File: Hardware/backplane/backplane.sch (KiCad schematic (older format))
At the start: 49 parts, among them J1 USB_B_Micro, SW1 SW_SPST, U1 74AC161, U2 MAX811SEUS-T, U3 MAX811SEUS-T, U4 PAL24, U5 74AC11, X1 24MHz

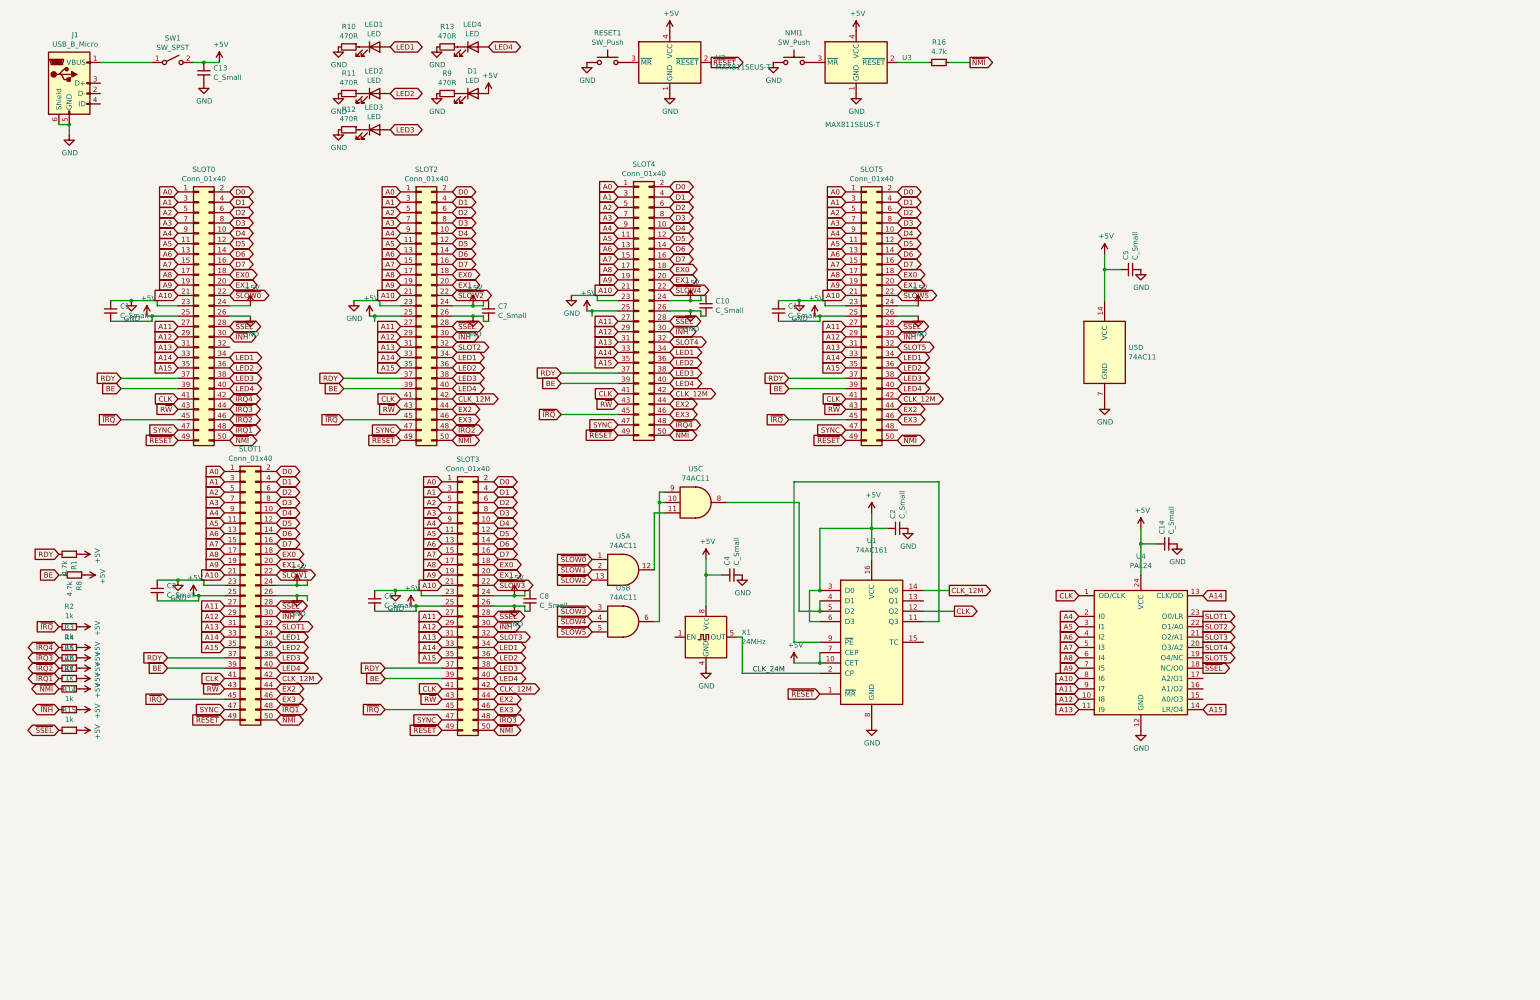
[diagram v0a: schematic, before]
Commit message: Many updates. SLOW signal is now shared amongst all slots, so their output has to be open drain.
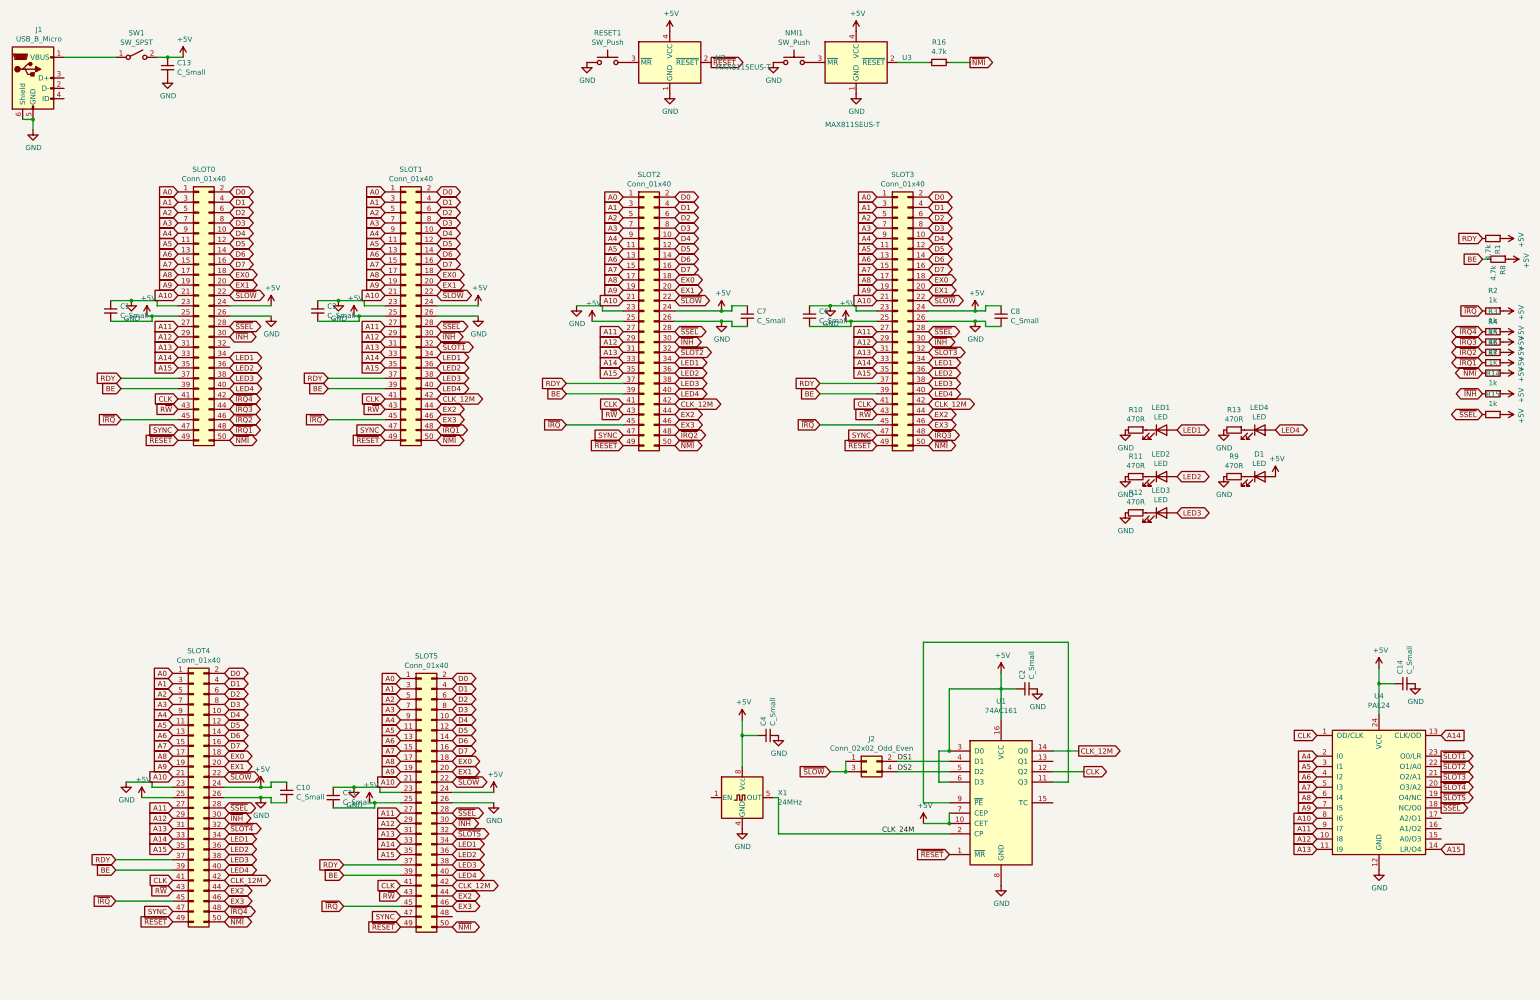
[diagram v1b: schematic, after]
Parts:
- removed C5: C_Small, Capacitor_SMD:C_1206_3216Metric_Pad1.42x1.75mm_HandSolder, symbol Device:C_Small
- removed U5: 74AC11, Package_SO:SOIC-14_3.9x8.7mm_P1.27mm, symbol 74xx:74LS11
- added J2: Conn_02x02_Odd_Even, Connector_PinHeader_2.54mm:PinHeader_2x02_P2.54mm_Vertical, symbol Connector_Generic:Conn_02x02_Odd_Even
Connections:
- net ~SLOW1~ is gone; now on net ~SLOW~: SLOT1.22 (Pin_22)
- net ~SLOW2~ is gone; now on net ~SLOW~: SLOT2.22 (Pin_22)
- net ~SLOW3~ is gone; now on net ~SLOW~: SLOT3.22 (Pin_22)
- net ~SLOW4~ is gone; now on net ~SLOW~: SLOT4.22 (Pin_22)
- net ~SLOW5~ is gone; now on net ~SLOW~: SLOT5.22 (Pin_22)
- net DS1: now reaches U1.4 (D1)
- net DS1: now also J2.2 (Pin_2); no longer U1.5 (D2)
- net SLOT1 renamed ~SLOT1~
- net SLOT2 renamed ~SLOT2~
- net SLOT3 renamed ~SLOT3~
- net SLOT4 renamed ~SLOT4~
- net SLOT5 renamed ~SLOT5~
- net ~SLOW0~ renamed ~SLOW~
- net ~SLOW~: now also J2.1 (Pin_1), J2.3 (Pin_3)
- new net DS2: J2.4 (Pin_4), U1.5 (D2)
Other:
- moved on the sheet: C10, C11, C13, C14, C2, C3, C4, C6, C7, C8, D1, J1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

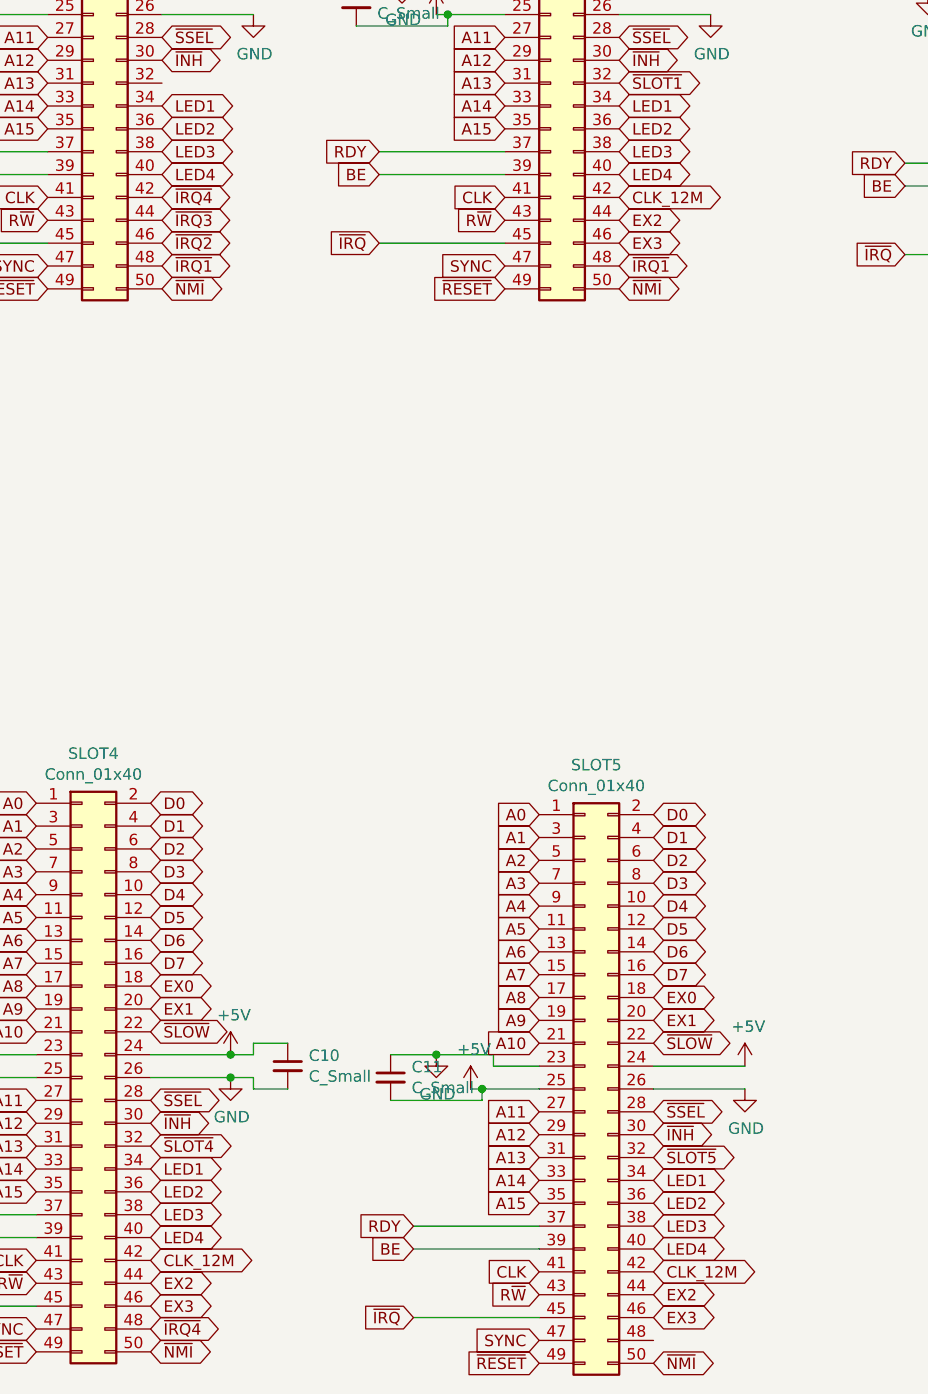
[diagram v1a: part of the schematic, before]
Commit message: Add IRQ signal for Slot 5
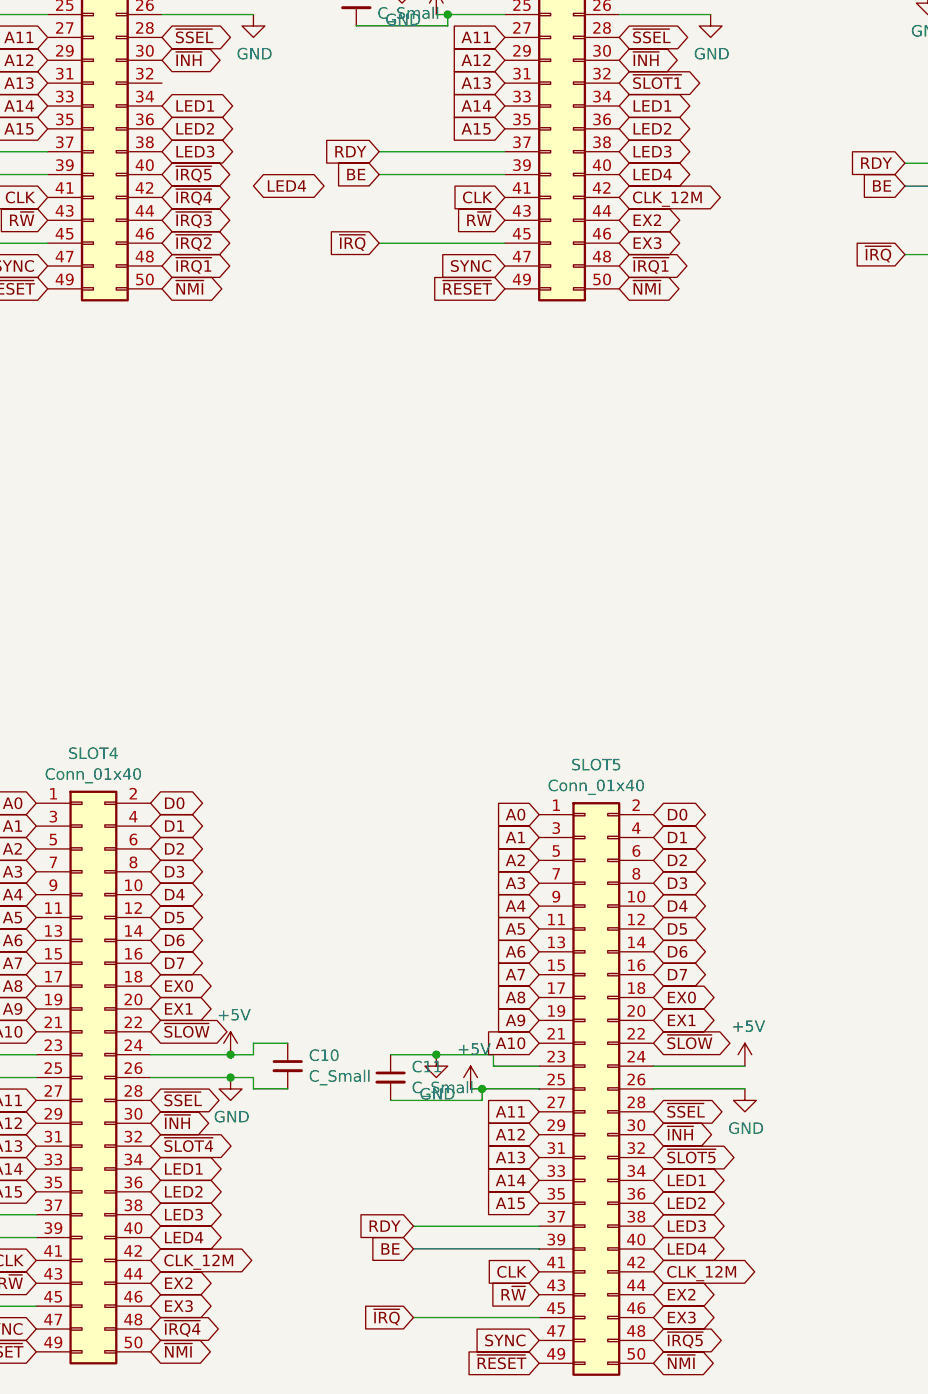
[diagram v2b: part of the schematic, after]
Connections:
- net LED4: no longer SLOT0.40 (Pin_40)
- net ~IRQ5~: now reaches SLOT5.48 (Pin_48)
- net ~IRQ5~: now also SLOT0.40 (Pin_40)
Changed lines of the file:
@@
 Text GLabel 2800 4150 2    50   BiDi ~ 0
 LED3
-Text GLabel 2800 4250 2    50   BiDi ~ 0
+Text GLabel 3200 4300 2    50   BiDi ~ 0
 LED4
 Text GLabel 2800 3150 2    50   BiDi ~ 0
@@
 Text Label 9250 7850 0    50   ~ 0
 DS1
+Text GLabel 2800 4250 2    50   BiDi ~ 0
+~IRQ5~
+Text GLabel 4950 9350 2    50   BiDi ~ 0
+~IRQ5~
 $EndSCHEMATC

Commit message: Backplane provides diode and pullups for SLOW signal
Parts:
- added D2, D3, D4, D5, D6, D7: DIODE, Diode_SMD:D_0805_2012Metric_Pad1.15x1.40mm_HandSolder, symbol pspice:DIODE
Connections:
- net ~IRQ~: no longer R2.2
- net ~SLOW~: now also R2.2, D2.1 (K), D3.1 (K), D4.1 (K), D5.1 (K), D6.1 (K), D7.1 (K); no longer SLOT0.22 (Pin_22), SLOT1.22 (Pin_22), SLOT2.22 (Pin_22), SLOT3.22 (Pin_22), SLOT4.22 (Pin_22), SLOT5.22 (Pin_22)
- new net: D3.2 (A), SLOT0.22 (Pin_22)
- new net: D6.2 (A), SLOT2.22 (Pin_22)
- new net: D2.2 (A), SLOT4.22 (Pin_22)
- new net: D5.2 (A), SLOT5.22 (Pin_22)
- new net: D4.2 (A), SLOT1.22 (Pin_22)
- new net: D7.2 (A), SLOT3.22 (Pin_22)
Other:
- note added: "Replace IRQ pull up with SLOW pullup"
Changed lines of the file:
@@
 ~IRQ1~
 Text GLabel 14900 3500 0    50   Input ~ 0
-~IRQ~
+~SLOW~
 Text GLabel 14900 2800 0    50   Input ~ 0
 RDY
@@
 Text GLabel 7100 3300 2    50   BiDi ~ 0
 EX1
-Text GLabel 7100 3400 2    50   BiDi ~ 0
-~SLOW~
 Text GLabel 7100 3800 2    50   BiDi ~ 0
 ~INH~
@@
 Text GLabel 12900 4650 2    50   BiDi ~ 0
 LED4
-Text GLabel 2800 3350 2    50   BiDi ~ 0
-~SLOW~
 Text GLabel 2800 3650 2    50   BiDi ~ 0
 ~SSEL~
-Text GLabel 2750 8000 2    50   BiDi ~ 0
-~SLOW~
 Text GLabel 2750 8400 2    50   BiDi ~ 0
 ~INH~
 Text GLabel 2750 8500 2    50   BiDi ~ 0
 ~SLOT4~
-Text GLabel 4950 8050 2    50   BiDi ~ 0
-~SLOW~
 Text GLabel 4950 8450 2    50   BiDi ~ 0
 ~INH~
 Text GLabel 4950 8550 2    50   BiDi ~ 0
 ~SLOT5~
-Text GLabel 9550 3400 2    50   BiDi ~ 0
+Text GLabel 10400 2950 2    50   BiDi ~ 0
 ~SLOW~
 Text GLabel 9550 3800 2    50   BiDi ~ 0
@@
 Text GLabel 9550 3900 2    50   BiDi ~ 0
 ~SLOT3~
-Text GLabel 4800 3350 2    50   BiDi ~ 0
-~SLOW~
 Text GLabel 4800 3750 2    50   BiDi ~ 0
 ~INH~
@@
 Text GLabel 4950 9350 2    50   BiDi ~ 0
 ~IRQ5~
+Text Notes 13150 3500 0    50   ~ 0
+Replace IRQ pull up with SLOW pullup
+$Comp
+L pspice:DIODE D7
+U 1 1 603C94D3
+P 10200 2950
+F 0 "D7" H 10200 2685 50  0000 C CNN
+F 1 "DIODE" H 10200 2776 50  0000 C CNN
+F 2 "Diode_SMD:D_0805_2012Metric_Pad1.15x1.40mm_HandSolder" H 10200 2950 50  0001 C CNN
+F 3 "~" H 10200 2950 50  0001 C CNN
+	1    10200 2950
+	-1   0    0    1
+$EndComp
+Wire Wire Line
+	10000 2950 9850 2950
+Wire Wire Line
+	9850 2950 9850 3400
+Wire Wire Line
+	9850 3400 9550 3400
+Text GLabel 7950 2950 2    50   BiDi ~ 0
+~SLOW~
+$Comp
+L pspice:DIODE D6
+U 1 1 603F44EB
+P 7750 2950
+F 0 "D6" H 7750 2685 50  0000 C CNN
+F 1 "DIODE" H 7750 2776 50  0000 C CNN
+F 2 "Diode_SMD:D_0805_2012Metric_Pad1.15x1.40mm_HandSolder" H 7750 2950 50  0001 C CNN
+F 3 "~" H 7750 2950 50  0001 C CNN
+	1    7750 2950
+	-1   0    0    1
+$EndComp
+Wire Wire Line
+	7550 2950 7400 2950
+Wire Wire Line
+	7400 2950 7400 3400
+Text GLabel 5650 2900 2    50   BiDi ~ 0
+~SLOW~
+$Comp
+L pspice:DIODE D4
+U 1 1 603F9D4C
+P 5450 2900
+F 0 "D4" H 5450 2635 50  0000 C CNN
+F 1 "DIODE" H 5450 2726 50  0000 C CNN
+F 2 "Diode_SMD:D_0805_2012Metric_Pad1.15x1.40mm_HandSolder" H 5450 2900 50  0001 C CNN
+F 3 "~" H 5450 2900 50  0001 C CNN
+	1    5450 2900
+	-1   0    0    1
+$EndComp
+Wire Wire Line
+	5250 2900 5100 2900
+Wire Wire Line
+	5100 2900 5100 3350
+Text GLabel 3650 2900 2    50   BiDi ~ 0
+~SLOW~
+Wire Wire Line
+	3100 2900 3100 3350
+Text GLabel 3550 7550 2    50   BiDi ~ 0
+~SLOW~
+$Comp
+L pspice:DIODE D2
+U 1 1 6040585B
+P 3350 7550
+F 0 "D2" H 3350 7285 50  0000 C CNN
+F 1 "DIODE" H 3350 7376 50  0000 C CNN
+F 2 "Diode_SMD:D_0805_2012Metric_Pad1.15x1.40mm_HandSolder" H 3350 7550 50  0001 C CNN
+F 3 "~" H 3350 7550 50  0001 C CNN
+	1    3350 7550
+	-1   0    0    1
+$EndComp
+Wire Wire Line
+	3150 7550 3000 7550
+Wire Wire Line
+	3000 7550 3000 8000
+Text GLabel 5750 7600 2    50   BiDi ~ 0
+~SLOW~
+$Comp
+L pspice:DIODE D5
+U 1 1 6040B971
+P 5550 7600
+F 0 "D5" H 5550 7335 50  0000 C CNN
+F 1 "DIODE" H 5550 7426 50  0000 C CNN
+F 2 "Diode_SMD:D_0805_2012Metric_Pad1.15x1.40mm_HandSolder" H 5550 7600 50  0001 C CNN
+F 3 "~" H 5550 7600 50  0001 C CNN
+	1    5550 7600
+	-1   0    0    1
+$EndComp
+Wire Wire Line
+	5350 7600 5200 7600
+Wire Wire Line
+	5200 7600 5200 8050
+Wire Wire Line
+	5200 8050 4950 8050
+Wire Wire Line
+	3000 8000 2750 8000
+Wire Wire Line
+	3100 3350 2800 3350
+Wire Wire Line
+	5100 3350 4800 3350
+Wire Wire Line
+	7400 3400 7100 3400
+Wire Wire Line
+	3250 2900 3100 2900
+$Comp
+L pspice:DIODE D3
+U 1 1 603FF9D8
+P 3450 2900
+F 0 "D3" H 3450 2635 50  0000 C CNN
+F 1 "DIODE" H 3450 2726 50  0000 C CNN
+F 2 "Diode_SMD:D_0805_2012Metric_Pad1.15x1.40mm_HandSolder" H 3450 2900 50  0001 C CNN
+F 3 "~" H 3450 2900 50  0001 C CNN
+	1    3450 2900
+	-1   0    0    1
+$EndComp
 $EndSCHEMATC

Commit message: small fixes on the hardware
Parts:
- added H1, H2, H3, H4: MountingHole_Pad, MountingHole:MountingHole_3.2mm_M3_Pad, symbol Mechanical:MountingHole_Pad
- added R17, R18: 1k, Resistor_SMD:R_0805_2012Metric_Pad1.15x1.40mm_HandSolder, symbol Device:R_Small
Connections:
- net +5V: now also R17.1, R18.1
- net DS1: now also R17.2
- net DS2: now also R18.2
- net GND: now also H1.1, H2.1, H3.1, H4.1
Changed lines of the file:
@@
 	3200 8200 3100 8200
 Connection ~ 3100 8200
-Text GLabel 8600 7950 0    50   Input ~ 0
+Text GLabel 8400 7950 0    50   Input ~ 0
 ~SLOW~
 $Comp
@@
 	8100 8550 9750 8550
 Wire Wire Line
-	8600 7950 8750 7950
-Wire Wire Line
 	8750 7950 8750 7850
 Connection ~ 8750 7950
 Wire Wire Line
-	9250 7950 9750 7950
+	9250 7950 9400 7950
 Wire Wire Line
 	9750 7850 9250 7850
@@
 	-1   0    0    1
 $EndComp
+$Comp
+L Device:R_Small R17
+U 1 1 6040FBAF
+P 9250 7550
+F 0 "R17" V 9054 7550 50  0000 C CNN
+F 1 "1k" V 9145 7550 50  0000 C CNN
+F 2 "Resistor_SMD:R_0805_2012Metric_Pad1.15x1.40mm_HandSolder" H 9250 7550 50  0001 C CNN
+F 3 "~" H 9250 7550 50  0001 C CNN
+	1    9250 7550
+	1    0    0    -1
+$EndComp
+$Comp
+L power:+5V #PWR0160
+U 1 1 60416782
+P 9250 7300
+F 0 "#PWR0160" H 9250 7150 50  0001 C CNN
+F 1 "+5V" H 9265 7473 50  0000 C CNN
+F 2 "" H 9250 7300 50  0001 C CNN
+F 3 "" H 9250 7300 50  0001 C CNN
+	1    9250 7300
+	1    0    0    -1
+$EndComp
+Wire Wire Line
+	9250 7650 9250 7850
+Wire Wire Line
+	9250 7300 9250 7450
+Connection ~ 9250 7850
+Wire Wire Line
+	8400 7950 8750 7950
+$Comp
+L Device:R_Small R18
+U 1 1 6043B47C
+P 9400 7650
+F 0 "R18" V 9204 7650 50  0000 C CNN
+F 1 "1k" V 9295 7650 50  0000 C CNN
+F 2 "Resistor_SMD:R_0805_2012Metric_Pad1.15x1.40mm_HandSolder" H 9400 7650 50  0001 C CNN
+F 3 "~" H 9400 7650 50  0001 C CNN
+	1    9400 7650
+	1    0    0    -1
+$EndComp
+$Comp
+L power:+5V #PWR0161
+U 1 1 6043B482
+P 9400 7400
+F 0 "#PWR0161" H 9400 7250 50  0001 C CNN
+F 1 "+5V" H 9415 7573 50  0000 C CNN
+F 2 "" H 9400 7400 50  0001 C CNN
+F 3 "" H 9400 7400 50  0001 C CNN
+	1    9400 7400
+	1    0    0    -1
+$EndComp
+Wire Wire Line
+	9400 7400 9400 7550
+Wire Wire Line
+	9400 7750 9400 7950
+Connection ~ 9400 7950
+Wire Wire Line
+	9400 7950 9750 7950
+$Comp
+L Mechanical:MountingHole_Pad H1
+U 1 1 604A8FFB
+P 7250 9750
+F 0 "H1" H 7350 9799 50  0000 L CNN
+F 1 "MountingHole_Pad" H 7350 9708 50  0000 L CNN
+F 2 "MountingHole:MountingHole_3.2mm_M3_Pad" H 7250 9750 50  0001 C CNN
+F 3 "~" H 7250 9750 50  0001 C CNN
+	1    7250 9750
+	1    0    0    -1
+$EndComp
+$Comp
+L Mechanical:MountingHole_Pad H2
+U 1 1 604B1566
+P 7650 9750
+F 0 "H2" H 7750 9799 50  0000 L CNN
+F 1 "MountingHole_Pad" H 7750 9708 50  0000 L CNN
+F 2 "MountingHole:MountingHole_3.2mm_M3_Pad" H 7650 9750 50  0001 C CNN
+F 3 "~" H 7650 9750 50  0001 C CNN
+	1    7650 9750
+	1    0    0    -1
+$EndComp
+$Comp
+L Mechanical:MountingHole_Pad H3
+U 1 1 604B8573
+P 8050 9750
+F 0 "H3" H 8150 9799 50  0000 L CNN
+F 1 "MountingHole_Pad" H 8150 9708 50  0000 L CNN
+F 2 "MountingHole:MountingHole_3.2mm_M3_Pad" H 8050 9750 50  0001 C CNN
+F 3 "~" H 8050 9750 50  0001 C CNN
+	1    8050 9750
+	1    0    0    -1
+$EndComp
+$Comp
+L Mechanical:MountingHole_Pad H4
+U 1 1 604BF521
+P 8450 9750
+F 0 "H4" H 8550 9799 50  0000 L CNN
+F 1 "MountingHole_Pad" H 8550 9708 50  0000 L CNN
+F 2 "MountingHole:MountingHole_3.2mm_M3_Pad" H 8450 9750 50  0001 C CNN
+F 3 "~" H 8450 9750 50  0001 C CNN
+	1    8450 9750
+	1    0    0    -1
+$EndComp
+Wire Wire Line
+	8450 9850 8050 9850
+Connection ~ 7650 9850
+Wire Wire Line
+	7650 9850 7250 9850
+Connection ~ 8050 9850
+Wire Wire Line
+	8050 9850 7650 9850
+$Comp
+L power:GND #PWR0162
+U 1 1 604CE063
+P 7650 9850
+F 0 "#PWR0162" H 7650 9600 50  0001 C CNN
+F 1 "GND" H 7655 9677 50  0000 C CNN
+F 2 "" H 7650 9850 50  0001 C CNN
+F 3 "" H 7650 9850 50  0001 C CNN
+	1    7650 9850
+	1    0    0    -1
+$EndComp
 $EndSCHEMATC
